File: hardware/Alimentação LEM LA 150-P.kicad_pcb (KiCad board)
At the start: 2 copper layers, 162 x 89 mm, 114 parts, among them J1 USART, J2 RJ45, J3 RJ45, J4 Conn_01x04, J5 Conn_01x04, U1 LM324, U4 ATMEGA328P-PU, U5 MCP2515-xSO, U6 MCP2551-I/SN, U7 LM7805, Y1 16MHz, Y2 16MHz

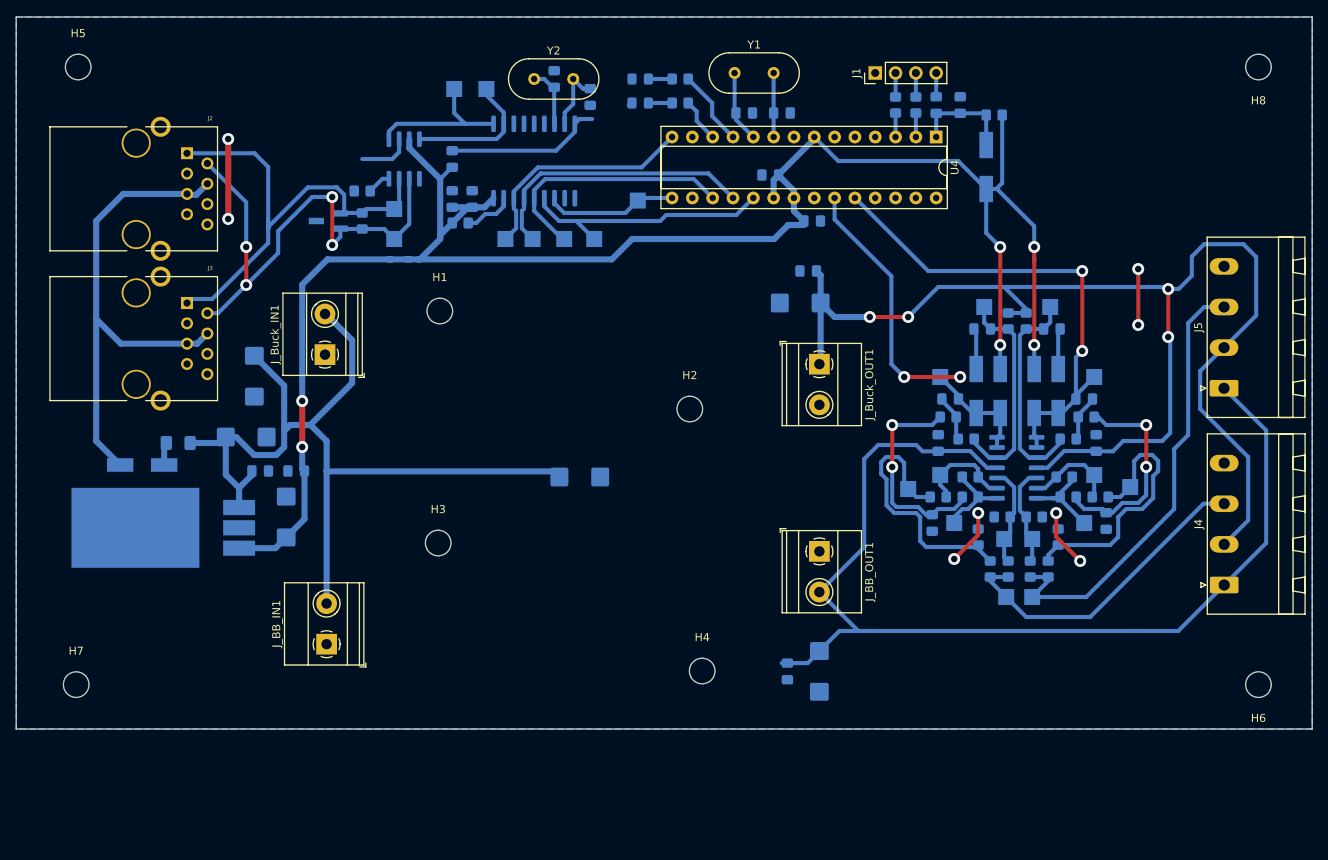
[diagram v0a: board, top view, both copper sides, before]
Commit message: Mudança do conversor 18V -> +/- 15V
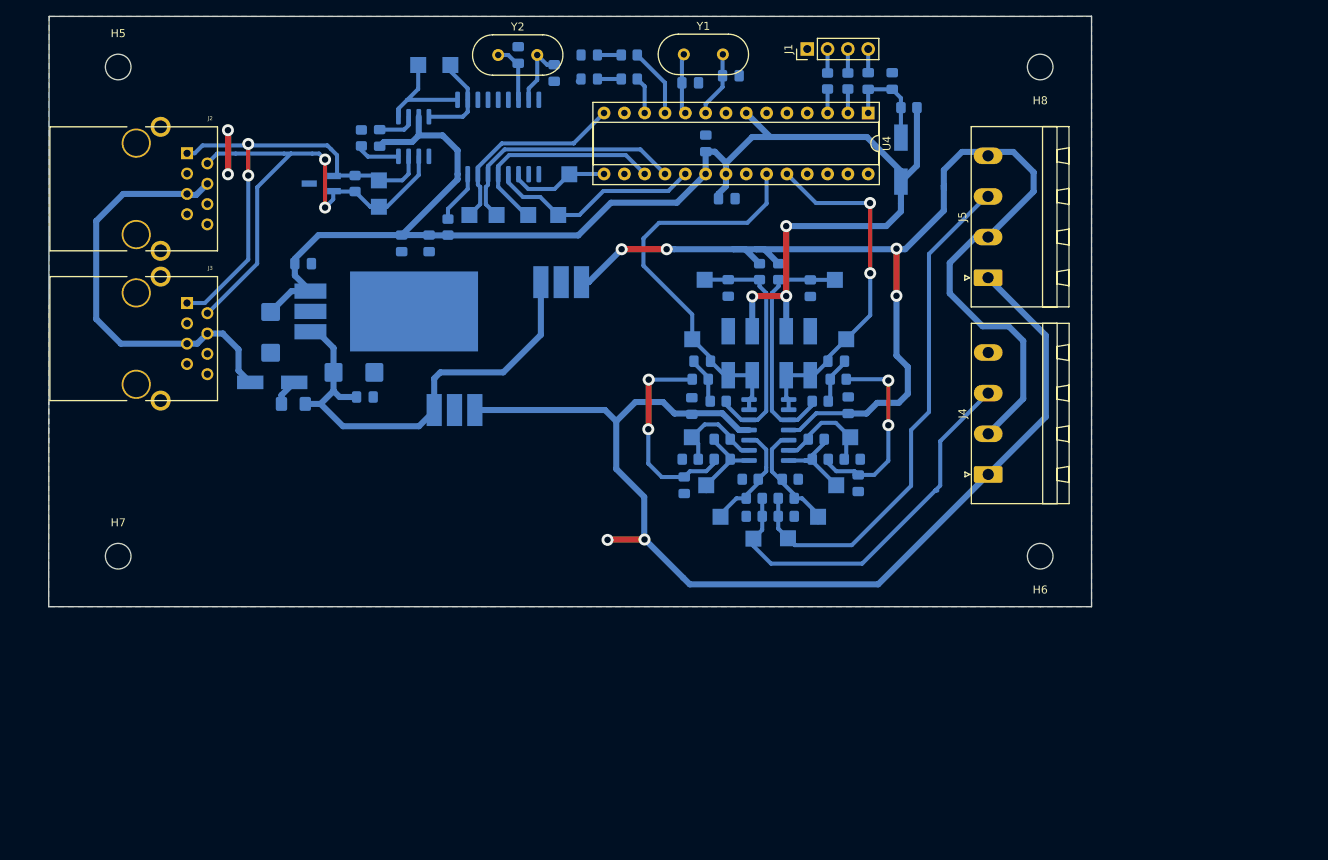
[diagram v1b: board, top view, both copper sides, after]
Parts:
- removed C1, C2: 100n, Capacitor_SMD:C_0805_2012Metric_Pad1.18x1.45mm_HandSolder
- removed C3, C4, C5, C6: 1u, Capacitor_Tantalum_SMD:CP_EIA-6032-20_AVX-F_Pad2.25x2.35mm_HandSolder
- removed H1: Buck_IN+, MountingHole:MountingHole_3.2mm_M3
- removed H2: Buck_Out-1, MountingHole:MountingHole_3.2mm_M3
- removed H3: BBoost_IN+1, MountingHole:MountingHole_3.2mm_M3
- removed H4: BBoost_Out-1, MountingHole:MountingHole_3.2mm_M3
- removed J_BB_IN1, J_BB_OUT1, J_Buck_IN1, J_Buck_OUT1: Screw_Terminal_01x02, TerminalBlock_Phoenix:TerminalBlock_Phoenix_MKDS-1,5-2-5.08_1x02_P5.08mm_Horizontal
- removed R1, R18: 100k, Resistor_SMD:R_0805_2012Metric_Pad1.20x1.40mm_HandSolder
- removed TP1, TP17: in-, TestPoint:TestPoint_Pad_2.0x2.0mm
- added U2: L7815, KicadZeniteSolarLibrary18:TO-220-3_Horizontal_Tabless_SMD, B.Cu at (100.6, 69.4)
- added U3: L7815, KicadZeniteSolarLibrary18:TO-220-3_Horizontal_Tabless_SMD, B.Cu at (87.2, 85.4)
- R23, R5: value 3k9 -> 1k
- moved TP4 35.6 mm to (123.0, 97.5)
- moved TP6 35.1 mm to (121.1, 67.8), turned to 90 degrees
- moved R19 33.4 mm to (131.3, 97.4), turned to 0 degrees
- moved R4 33.0 mm to (127.3, 95.2), turned to 0 degrees
- moved J4 32.6 mm to (156.5, 92.2)
- moved J5 32.6 mm to (156.5, 67.6)
- moved TP2 32.4 mm to (127.2, 100.2)
- moved C12 32.2 mm to (124.0, 68.9), turned to -90 degrees
- moved R6 31.8 mm to (126.8, 92.8)
- moved R21 31.8 mm to (131.3, 95.2), turned to 180 degrees
- moved R27 31.7 mm to (127.9, 66.8)
- moved H6 31.7 mm to (163.0, 102.4)
- moved R28 31.6 mm to (130.3, 66.8)
- moved TP3 31.4 mm to (119.5, 87.5)
- moved TP18 31.4 mm to (131.5, 100.2)
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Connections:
- net /Buck e BuckBoost/+18V_IN renamed /POWER SUPPLY/+18V_OUT
- net /CANBUS/CS renamed /MCU/MCP_SS
- net /CANBUS/INT renamed /MCU/MCP_INT
- net /MCU/analog1 renamed /Bipolar Analog/out1
- net /MCU/analog2 renamed /Bipolar Analog/out2
- net /POWER SUPPLY/+18V_IN renamed /CANBUS CONN/CAN_18V
- R19 pad 2: Net-(R18-Pad1) -> GND
- R2 pad 2: Net-(R1-Pad1) -> GND
- R20 pad 2: Net-(R18-Pad1) -> GND
- R3 pad 2: Net-(R1-Pad1) -> GND
- U4 pad 13: Net-(U4-Pad13) -> unconnected-(U4-Pad13)
- U4 pad 16: Net-(U4-Pad16) -> unconnected-(U4-Pad16)
- U4 pad 25: Net-(U4-Pad25) -> unconnected-(U4-Pad25)
- U4 pad 26: Net-(U4-Pad26) -> unconnected-(U4-Pad26)
- U4 pad 27: Net-(U4-Pad27) -> unconnected-(U4-Pad27)
- U4 pad 28: Net-(U4-Pad28) -> unconnected-(U4-Pad28)
- U4 pad 4: Net-(U4-Pad4) -> unconnected-(U4-Pad4)
- U4 pad 5: Net-(U4-Pad5) -> unconnected-(U4-Pad5)
- U4 pad 6: Net-(U4-Pad6) -> unconnected-(U4-Pad6)
- U5 pad 10: Net-(U5-Pad10) -> unconnected-(U5-Pad10)
- U5 pad 11: Net-(U5-Pad11) -> unconnected-(U5-Pad11)
- U5 pad 3: Net-(U5-Pad3) -> unconnected-(U5-Pad3)
- U5 pad 4: Net-(U5-Pad4) -> unconnected-(U5-Pad4)
- U5 pad 5: Net-(U5-Pad5) -> unconnected-(U5-Pad5)
- U5 pad 6: Net-(U5-Pad6) -> unconnected-(U5-Pad6)
- U6 pad 5: Net-(U6-Pad5) -> unconnected-(U6-Pad5)
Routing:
- net GND: track 68.8 -> 12.2 mm, vias 8 -> 2
- net +5V: track 241.7 -> 186.0 mm, vias 6 -> 3
- net /POWER SUPPLY/+18V_OUT: track 113.6 -> 58.9 mm
- net Net-(R18-Pad1): track 33.5 -> 0.00 mm
- net Net-(R1-Pad1): track 33.5 -> 0.00 mm
- net /Bipolar Analog/out2: track 63.2 -> 44.9 mm
- net /CANBUS CONN/CAN_18V: track 63.4 -> 53.8 mm
- net /Bipolar Analog/in1+: track 39.7 -> 49.0 mm
- net /Bipolar Analog/in2+: track 57.2 -> 64.6 mm
- net /CANBUS/TXCAN: track 19.4 -> 13.8 mm
- net /CANBUS/RXCAN: track 17.2 -> 11.9 mm
- net /SCK: track 32.3 -> 27.0 mm
- net -15V: track 135.4 -> 139.7 mm, vias 0 -> 2
- net /MOSI: track 31.7 -> 27.7 mm
- net /MISO: track 35.0 -> 31.0 mm
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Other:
- board size 162 x 89 mm -> 130.4 x 73.8 mm
- net class Default removed

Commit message: Troca do atmega328p -> STM32F103C8T Já que tem CAN integrado e ADC 12 bits (ao invés de 10)
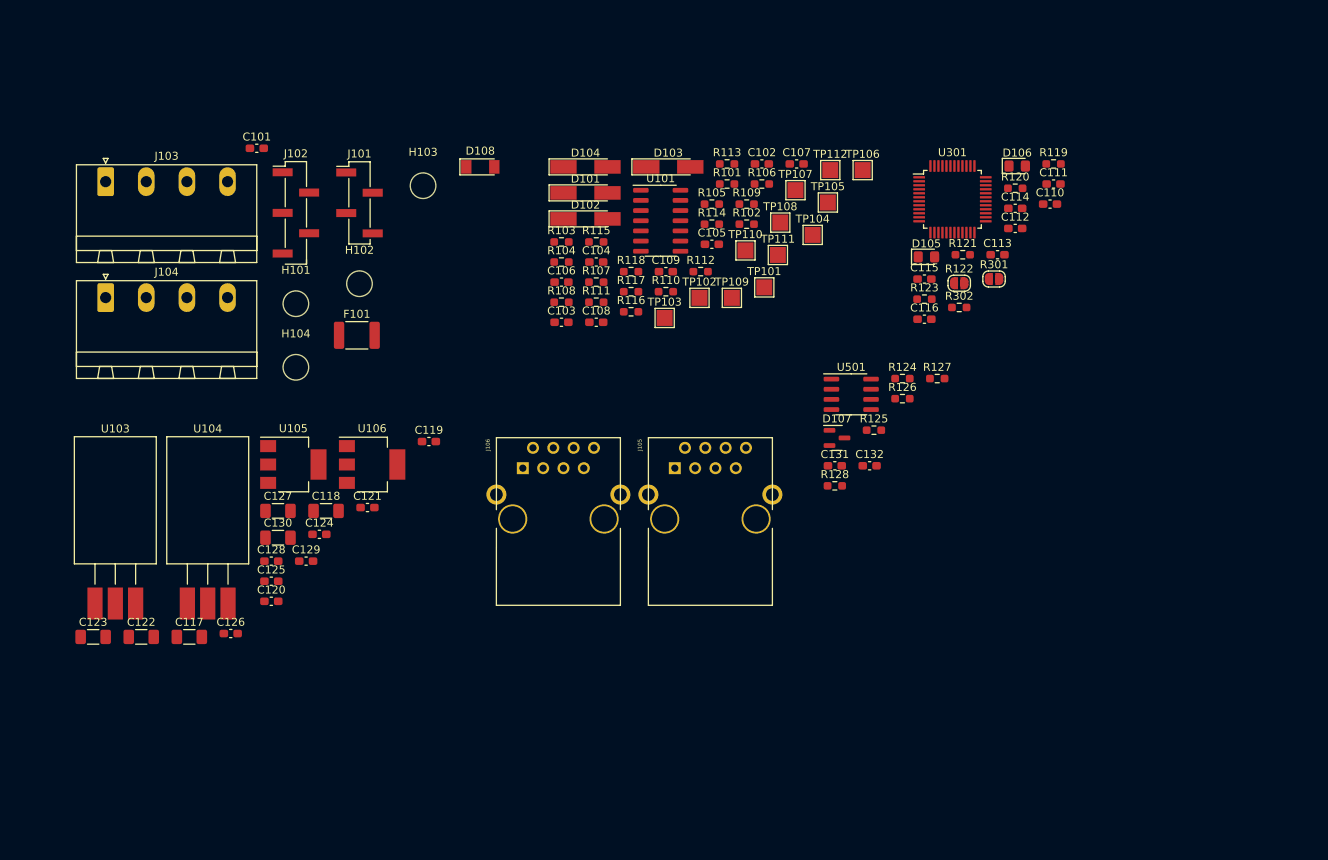
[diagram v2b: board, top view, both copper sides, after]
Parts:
- removed C10, C11, C12, C13, C29, C30, C31, C7: 100n, Capacitor_SMD:C_0805_2012Metric_Pad1.18x1.45mm_HandSolder
- removed C14, C15, C16, C17, C22, C23, C24, C25, C26: 100nF, Capacitor_SMD:C_0805_2012Metric_Pad1.18x1.45mm_HandSolder
- removed C18, C19, C20, C21: 22pF, Capacitor_SMD:C_0805_2012Metric_Pad1.18x1.45mm_HandSolder
- removed C27, C28: 1u, Capacitor_Tantalum_SMD:CP_EIA-6032-20_AVX-F_Pad2.25x2.35mm_HandSolder
- removed D1: pesd1can, Package_TO_SOT_SMD:SOT-23_Handsoldering
- removed D2, D7, D8, D9: 4V7, Diode_SMD:D_MiniMELF_Handsoldering
- removed D3, D6: LL4148, Diode_SMD:D_MiniMELF_Handsoldering
- removed D4, D5: LED_RED, LED_SMD:LED_0805_2012Metric_Pad1.15x1.40mm_HandSolder
- removed F1: 500mA, Fuse:Fuse_1206_3216Metric_Pad1.42x1.75mm_HandSolder
- removed H5: Mount_TL, MountingHole:MountingHole_3.2mm_M3
- removed H6: Mount_TR, MountingHole:MountingHole_3.2mm_M3
- removed H7: Mount_BL, MountingHole:MountingHole_3.2mm_M3
- removed H8: Mount_BR, MountingHole:MountingHole_3.2mm_M3
- removed J1: USART, Connector_PinHeader_2.54mm:PinHeader_1x04_P2.54mm_Vertical
- removed J2, J3: RJ45, KicadZeniteSolarLibrary18:RJ45_YH59_01
- removed J4, J5: Conn_01x04, Connector_Phoenix_MSTB:PhoenixContact_MSTBA_2,5_4-G-5,08_1x04_P5.08mm_Horizontal
- removed R10, R12, R13, R14, R20, R21, R23, R24, R25, R26, R3, R4, R5, R7, R8, R9: 1k, Resistor_SMD:R_0805_2012Metric_Pad1.20x1.40mm_HandSolder
- removed R11, R15: 10k, Resistor_SMD:R_0805_2012Metric_Pad1.20x1.40mm_HandSolder
- removed R16: 4k7, Resistor_SMD:R_0805_2012Metric_Pad1.20x1.40mm_HandSolder
- removed R17: 120, Resistor_SMD:R_0805_2012Metric_Pad1.20x1.40mm_HandSolder
- removed R19, R2: 30, Resistor_SMD:R_0805_2012Metric_Pad1.20x1.40mm_HandSolder
- removed R22, R6: 3k9, Resistor_SMD:R_0805_2012Metric_Pad1.20x1.40mm_HandSolder
- removed R27, R28: 15k, Resistor_SMD:R_0805_2012Metric_Pad1.20x1.40mm_HandSolder
- removed TP10: SO, TestPoint:TestPoint_Pad_2.0x2.0mm
- removed TP11: SI, TestPoint:TestPoint_Pad_2.0x2.0mm
- removed TP12: INT, TestPoint:TestPoint_Pad_2.0x2.0mm
- removed TP13: TXCAN, TestPoint:TestPoint_Pad_2.0x2.0mm
- removed TP14: RXCAN, TestPoint:TestPoint_Pad_2.0x2.0mm
- removed TP15: CAN_H, TestPoint:TestPoint_Pad_2.0x2.0mm
- removed TP16: CAN_L, TestPoint:TestPoint_Pad_2.0x2.0mm
- removed TP18, TP2: in+, TestPoint:TestPoint_Pad_2.0x2.0mm
- removed TP19, TP3: op_a_in-, TestPoint:TestPoint_Pad_2.0x2.0mm
- removed TP20, TP4: op_a_in+, TestPoint:TestPoint_Pad_2.0x2.0mm
- removed TP21, TP5: op_a_out, TestPoint:TestPoint_Pad_2.0x2.0mm
- removed TP22, TP6: op_b_in+, TestPoint:TestPoint_Pad_2.0x2.0mm
- removed TP23, TP7: op_b_out, TestPoint:TestPoint_Pad_2.0x2.0mm
- removed TP8: SCK, TestPoint:TestPoint_Pad_2.0x2.0mm
- removed TP9: SC, TestPoint:TestPoint_Pad_2.0x2.0mm
- removed U1: LM324, Package_SO:SOIC-14_3.9x8.7mm_P1.27mm
- removed U2, U3: L7815, KicadZeniteSolarLibrary18:TO-220-3_Horizontal_Tabless_SMD
- removed U4: ATMEGA328P-PU, Package_DIP:DIP-28_W7.62mm_Socket
- removed U5: MCP2515-xSO, Package_SO:SOIC-18W_7.5x11.6mm_P1.27mm
- removed U6: MCP2551-I/SN, Package_SO:SOIC-8_3.9x4.9mm_P1.27mm
- removed U7: LM7805, KicadZeniteSolarLibrary18:TO-220-3_Horizontal_TabDown_SMD
- removed Y1, Y2: 16MHz, Crystal:Crystal_HC49-U_Vertical
- added C101: 100n, Capacitor_SMD:C_0603_1608Metric_Pad1.08x0.95mm_HandSolder, F.Cu at (65.1, 51.4)
- added C102: 100n, Capacitor_SMD:C_0603_1608Metric_Pad1.08x0.95mm_HandSolder, F.Cu at (128.2, 53.4)
- added C103: 100n, Capacitor_SMD:C_0603_1608Metric_Pad1.08x0.95mm_HandSolder, F.Cu at (103.2, 73.2)
- added C104: 100n, Capacitor_SMD:C_0603_1608Metric_Pad1.08x0.95mm_HandSolder, F.Cu at (107.5, 65.6)
- added C105: 100n, Capacitor_SMD:C_0603_1608Metric_Pad1.08x0.95mm_HandSolder, F.Cu at (122.0, 63.4)
- added C106: 100n, Capacitor_SMD:C_0603_1608Metric_Pad1.08x0.95mm_HandSolder, F.Cu at (103.2, 68.1)
- added C107: 100n, Capacitor_SMD:C_0603_1608Metric_Pad1.08x0.95mm_HandSolder, F.Cu at (132.6, 53.4)
- added C108: 100n, Capacitor_SMD:C_0603_1608Metric_Pad1.08x0.95mm_HandSolder, F.Cu at (107.5, 73.2)
- added C109: 100n, Capacitor_SMD:C_0603_1608Metric_Pad1.08x0.95mm_HandSolder, F.Cu at (116.2, 66.8)
- added C110: 100n, Capacitor_SMD:C_0603_1608Metric_Pad1.08x0.95mm_HandSolder, F.Cu at (164.2, 58.4)
- added C111: 100n, Capacitor_SMD:C_0603_1608Metric_Pad1.08x0.95mm_HandSolder, F.Cu at (164.7, 55.9)
- added C112: 100n, Capacitor_SMD:C_0603_1608Metric_Pad1.08x0.95mm_HandSolder, F.Cu at (159.9, 61.4)
- added C113: 100n, Capacitor_SMD:C_0603_1608Metric_Pad1.08x0.95mm_HandSolder, F.Cu at (157.7, 64.7)
- added C114: 100n, Capacitor_SMD:C_0603_1608Metric_Pad1.08x0.95mm_HandSolder, F.Cu at (159.9, 58.9)
- added C115: 100n, Capacitor_SMD:C_0603_1608Metric_Pad1.08x0.95mm_HandSolder, F.Cu at (148.5, 67.8)
- added C116: 100n, Capacitor_SMD:C_0603_1608Metric_Pad1.08x0.95mm_HandSolder, F.Cu at (148.5, 72.8)
- added C117: 4.7u, Capacitor_SMD:C_1206_3216Metric_Pad1.33x1.80mm_HandSolder, F.Cu at (56.6, 112.5)
- added C118: 4.7u, Capacitor_SMD:C_1206_3216Metric_Pad1.33x1.80mm_HandSolder, F.Cu at (73.7, 96.7)
- added C119: 100n, Capacitor_SMD:C_0603_1608Metric_Pad1.08x0.95mm_HandSolder, F.Cu at (86.6, 88.1)
- added C120: 100n, Capacitor_SMD:C_0603_1608Metric_Pad1.08x0.95mm_HandSolder, F.Cu at (66.9, 108.0)
- added C121: 100n, Capacitor_SMD:C_0603_1608Metric_Pad1.08x0.95mm_HandSolder, F.Cu at (78.9, 96.3)
- added C122: 4.7u, Capacitor_SMD:C_1206_3216Metric_Pad1.33x1.80mm_HandSolder, F.Cu at (50.6, 112.5)
- added C123: 4.7u, Capacitor_SMD:C_1206_3216Metric_Pad1.33x1.80mm_HandSolder, F.Cu at (44.6, 112.5)
- added C124: 100n, Capacitor_SMD:C_0603_1608Metric_Pad1.08x0.95mm_HandSolder, F.Cu at (72.9, 99.7)
- added C125: 100n, Capacitor_SMD:C_0603_1608Metric_Pad1.08x0.95mm_HandSolder, F.Cu at (66.9, 105.5)
- added C126: 100n, Capacitor_SMD:C_0603_1608Metric_Pad1.08x0.95mm_HandSolder, F.Cu at (61.8, 112.1)
- added C127: 4.7u, Capacitor_SMD:C_1206_3216Metric_Pad1.33x1.80mm_HandSolder, F.Cu at (67.7, 96.7)
- added C128: 100n, Capacitor_SMD:C_0603_1608Metric_Pad1.08x0.95mm_HandSolder, F.Cu at (66.9, 103.0)
- added C129: 100n, Capacitor_SMD:C_0603_1608Metric_Pad1.08x0.95mm_HandSolder, F.Cu at (71.2, 103.0)
- added C130: 4.7u, Capacitor_SMD:C_1206_3216Metric_Pad1.33x1.80mm_HandSolder, F.Cu at (67.7, 100.1)
- added C131: 100n, Capacitor_SMD:C_0603_1608Metric_Pad1.08x0.95mm_HandSolder, F.Cu at (137.3, 91.1)
- added C132: 4.7n, Capacitor_SMD:C_0603_1608Metric_Pad1.08x0.95mm_HandSolder, F.Cu at (141.7, 91.1)
- added D101: 3V9, Diode_SMD:D_MiniMELF_Handsoldering, F.Cu at (106.2, 57.0)
- added D102: 3V9, Diode_SMD:D_MiniMELF_Handsoldering, F.Cu at (106.2, 60.2)
- added D103: 3V9, Diode_SMD:D_MiniMELF_Handsoldering, F.Cu at (116.5, 53.7)
- added D104: 3V9, Diode_SMD:D_MiniMELF_Handsoldering, F.Cu at (106.2, 53.7)
- added D105: ~, LED_SMD:LED_0805_2012Metric_Pad1.15x1.40mm_HandSolder, F.Cu at (148.8, 65.0)
- added D106: ~, LED_SMD:LED_0805_2012Metric_Pad1.15x1.40mm_HandSolder, F.Cu at (160.1, 53.6)
- added D107: ~, Package_TO_SOT_SMD:SOT-23, F.Cu at (137.6, 87.6)
- added D108: LL4148, Diode_SMD:D_MiniMELF, F.Cu at (93.0, 53.7)
- added F101: Fuse, Fuse:Fuse_1812_4532Metric_Pad1.30x3.40mm_HandSolder, F.Cu at (77.6, 74.8)
- added H101: Mount_TL, MountingHole:MountingHole_3.2mm_M3, F.Cu at (70.0, 70.8)
- added H102: Mount_TR, MountingHole:MountingHole_3.2mm_M3, F.Cu at (77.9, 68.3)
- added H103: Mount_BL, MountingHole:MountingHole_3.2mm_M3, F.Cu at (85.9, 56.1)
- added H104: Mount_BR, MountingHole:MountingHole_3.2mm_M3, F.Cu at (70.0, 78.8)
- added J101: USART, Connector_PinHeader_2.54mm:PinHeader_1x04_P2.54mm_Vertical_SMD_Pin1Left, F.Cu at (77.9, 58.2)
- added J102: STLink, Connector_PinHeader_2.54mm:PinHeader_1x05_P2.54mm_Vertical_SMD_Pin1Left, F.Cu at (70.0, 59.5)
- added J103: Sensor1, Connector_Phoenix_MSTB:PhoenixContact_MSTBA_2,5_4-G-5,08_1x04_P5.08mm_Horizontal, F.Cu at (46.2, 55.6)
- added J104: Sensor2, Connector_Phoenix_MSTB:PhoenixContact_MSTBA_2,5_4-G-5,08_1x04_P5.08mm_Horizontal, F.Cu at (46.2, 70.1)
- added J105: RJ45, KicadZeniteSolarLibrary18:RJ45_YH59_01, F.Cu at (117.3, 91.4)
- added J106: RJ45, KicadZeniteSolarLibrary18:RJ45_YH59_01, F.Cu at (98.3, 91.4)
- added R101: 30, Resistor_SMD:R_0603_1608Metric_Pad0.98x0.95mm_HandSolder, F.Cu at (123.9, 55.9)
- added R102: 30, Resistor_SMD:R_0603_1608Metric_Pad0.98x0.95mm_HandSolder, F.Cu at (126.3, 60.9)
- added R103: 1k, Resistor_SMD:R_0603_1608Metric_Pad0.98x0.95mm_HandSolder, F.Cu at (103.2, 63.1)
- added R104: 1k, Resistor_SMD:R_0603_1608Metric_Pad0.98x0.95mm_HandSolder, F.Cu at (103.2, 65.6)
- added R105: 1k, Resistor_SMD:R_0603_1608Metric_Pad0.98x0.95mm_HandSolder, F.Cu at (122.0, 58.4)
- added R106: 1k, Resistor_SMD:R_0603_1608Metric_Pad0.98x0.95mm_HandSolder, F.Cu at (128.2, 55.9)
- added R107: 1k, Resistor_SMD:R_0603_1608Metric_Pad0.98x0.95mm_HandSolder, F.Cu at (107.5, 68.1)
- added R108: 3k9, Resistor_SMD:R_0603_1608Metric_Pad0.98x0.95mm_HandSolder, F.Cu at (103.2, 70.6)
- added R109: 3k9, Resistor_SMD:R_0603_1608Metric_Pad0.98x0.95mm_HandSolder, F.Cu at (126.3, 58.4)
- added R110: 1k, Resistor_SMD:R_0603_1608Metric_Pad0.98x0.95mm_HandSolder, F.Cu at (116.2, 69.3)
- added R111: 1k, Resistor_SMD:R_0603_1608Metric_Pad0.98x0.95mm_HandSolder, F.Cu at (107.5, 70.6)
- added R112: 1k, Resistor_SMD:R_0603_1608Metric_Pad0.98x0.95mm_HandSolder, F.Cu at (120.6, 66.8)
- added R113: 1k, Resistor_SMD:R_0603_1608Metric_Pad0.98x0.95mm_HandSolder, F.Cu at (123.9, 53.4)
- added R114: 1k, Resistor_SMD:R_0603_1608Metric_Pad0.98x0.95mm_HandSolder, F.Cu at (122.0, 60.9)
- added R115: 1k, Resistor_SMD:R_0603_1608Metric_Pad0.98x0.95mm_HandSolder, F.Cu at (107.5, 63.1)
- added R116: 1k, Resistor_SMD:R_0603_1608Metric_Pad0.98x0.95mm_HandSolder, F.Cu at (111.9, 71.8)
- added R117: 15k, Resistor_SMD:R_0603_1608Metric_Pad0.98x0.95mm_HandSolder, F.Cu at (111.9, 69.3)
- added R118: 15k, Resistor_SMD:R_0603_1608Metric_Pad0.98x0.95mm_HandSolder, F.Cu at (111.9, 66.8)
- added R119: 10k, Resistor_SMD:R_0603_1608Metric_Pad0.98x0.95mm_HandSolder, F.Cu at (164.7, 53.4)
- added R120: 10k, Resistor_SMD:R_0603_1608Metric_Pad0.98x0.95mm_HandSolder, F.Cu at (159.9, 56.4)
- added R121: 10k, Resistor_SMD:R_0603_1608Metric_Pad0.98x0.95mm_HandSolder, F.Cu at (153.3, 64.7)
- added R122: BOOT0, Jumper:SolderJumper-2_P1.3mm_Open_RoundedPad1.0x1.5mm, F.Cu at (152.9, 68.3)
- added R123: 10k, Resistor_SMD:R_0603_1608Metric_Pad0.98x0.95mm_HandSolder, F.Cu at (148.5, 70.3)
- added R124: 4k7, Resistor_SMD:R_0603_1608Metric_Pad0.98x0.95mm_HandSolder, F.Cu at (145.8, 80.2)
- added R125: NC, Resistor_SMD:R_0603_1608Metric_Pad0.98x0.95mm_HandSolder, F.Cu at (142.2, 86.6)
- added R126: 300, Resistor_SMD:R_0603_1608Metric_Pad0.98x0.95mm_HandSolder, F.Cu at (145.8, 82.7)
- added R127: 520, Resistor_SMD:R_0603_1608Metric_Pad0.98x0.95mm_HandSolder, F.Cu at (150.1, 80.2)
- added R128: 520, Resistor_SMD:R_0603_1608Metric_Pad0.98x0.95mm_HandSolder, F.Cu at (137.3, 93.6)
- added R301: JUMP0, Jumper:SolderJumper-2_P1.3mm_Open_RoundedPad1.0x1.5mm, F.Cu at (157.2, 67.7)
- added R302: 10k, Resistor_SMD:R_0603_1608Metric_Pad0.98x0.95mm_HandSolder, F.Cu at (152.9, 71.3)
- added TP101: in+, TestPoint:TestPoint_Pad_2.0x2.0mm, F.Cu at (128.5, 68.8)
- added TP102: in+, TestPoint:TestPoint_Pad_2.0x2.0mm, F.Cu at (120.4, 70.1)
- added TP103: op_a_in-, TestPoint:TestPoint_Pad_2.0x2.0mm, F.Cu at (116.1, 72.6)
- added TP104: op_a_in+, TestPoint:TestPoint_Pad_2.0x2.0mm, F.Cu at (134.6, 62.2)
- added TP105: op_a_in-, TestPoint:TestPoint_Pad_2.0x2.0mm, F.Cu at (136.5, 58.2)
- added TP106: op_a_in+, TestPoint:TestPoint_Pad_2.0x2.0mm, F.Cu at (140.8, 54.1)
- added TP107: op_a_out, TestPoint:TestPoint_Pad_2.0x2.0mm, F.Cu at (132.4, 56.6)
- added TP108: op_a_out, TestPoint:TestPoint_Pad_2.0x2.0mm, F.Cu at (130.5, 60.7)
- added TP109: op_b_in+, TestPoint:TestPoint_Pad_2.0x2.0mm, F.Cu at (124.5, 70.1)
- added TP110: op_b_in+, TestPoint:TestPoint_Pad_2.0x2.0mm, F.Cu at (126.2, 64.2)
- added TP111: op_b_out, TestPoint:TestPoint_Pad_2.0x2.0mm, F.Cu at (130.2, 64.7)
- added TP112: op_b_out, TestPoint:TestPoint_Pad_2.0x2.0mm, F.Cu at (136.8, 54.1)
- added U101: LM324, Package_SO:SOIC-14_3.9x8.7mm_P1.27mm, F.Cu at (115.6, 60.5)
- added U103: K78L15-1000R3, KicadZeniteSolarLibrary18:TO-220-3_Horizontal_Tabless_SMD, F.Cu at (44.8, 107.0)
- added U104: K78L15-1000R3, KicadZeniteSolarLibrary18:TO-220-3_Horizontal_Tabless_SMD, F.Cu at (56.4, 107.0)
- added U105: AMS1117-5, Package_TO_SOT_SMD:SOT-223-3_TabPin2, F.Cu at (69.6, 90.9)
- added U106: AMS1117-3.3, Package_TO_SOT_SMD:SOT-223-3_TabPin2, F.Cu at (79.5, 90.9)
- added U301: STM32F103C8Tx, Package_QFP:LQFP-48_7x7mm_P0.5mm, F.Cu at (152.0, 57.8)
- added U501: MCP2561-E-SN, Package_SO:SOIC-8_3.9x4.9mm_P1.27mm, F.Cu at (139.4, 82.2)
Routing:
- net +5V: track 186.0 -> 0.00 mm, vias 3 -> 0
- net +15V: track 156.7 -> 0.00 mm, vias 4 -> 0
- net -15V: track 139.7 -> 0.00 mm, vias 2 -> 0
- net /Bipolar Analog/in2+: track 64.6 -> 0.00 mm
- net /CANBUS CONN/CAN_L: track 63.8 -> 0.00 mm, vias 2 -> 0
- net /CANBUS CONN/CAN_H: track 60.7 -> 0.00 mm, vias 2 -> 0
- net /POWER SUPPLY/+18V_OUT: track 58.9 -> 0.00 mm
- net /CANBUS CONN/CAN_18V: track 53.8 -> 0.00 mm
- net /Bipolar Analog/out1: track 50.4 -> 0.00 mm
- net /Bipolar Analog/in1+: track 49.0 -> 0.00 mm
- net /Bipolar Analog/out2: track 44.9 -> 0.00 mm, vias 2 -> 0
- net Net-(C31-Pad1): track 31.4 -> 0.00 mm
- net /MISO: track 31.0 -> 0.00 mm
- net Net-(C12-Pad1): track 30.3 -> 0.00 mm
- net /MOSI: track 27.7 -> 0.00 mm
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- removed copper zone on B.Cu, net GND
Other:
- board outline removed

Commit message: Primeiro protótipo da PCB
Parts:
- added TP501: TxCAN, TestPoint:TestPoint_Pad_2.0x2.0mm, B.Cu at (125.1, 72.4)
- added TP502: RxCAN, TestPoint:TestPoint_Pad_2.0x2.0mm, B.Cu at (126.4, 75.6)
- added TP503: CAN_H, TestPoint:TestPoint_Pad_2.0x2.0mm, B.Cu at (118.9, 84.8)
- added TP504: CAN_L, TestPoint:TestPoint_Pad_2.0x2.0mm, B.Cu at (124.0, 84.8)
- C102, C103, C104, C105, C106, C107, C108, C109, C110, C111, C112, C113, C114, C115, C116, C118, C120, C123, C125, C131, C132, D101, D102, D103, D104, D105, D106, R101, R102, R103, R104, R105, R106, R107, R108, R109, R110, R111, R112, R113, R114, R115, R116, R117, R118, R119, R120, R121, R122, R123, R124, R125, R126, R127, R128, R301, R302, TP101, TP102, TP103, TP104, TP105, TP106, TP107, TP108, TP109, TP110, TP111, TP112, U101, U104, U301, U501: moved to B.Cu
- D107: value ~ -> pesd1can; moved to B.Cu
- moved J104 147.4 mm to (184.9, 119.9), turned to 90 degrees
- moved J103 143.8 mm to (184.9, 93.5), turned to 90 degrees
- moved H104 131.1 mm to (190.5, 130.5)
- moved H103 105.2 mm to (190.5, 67.2)
- moved C101 90.3 mm to (151.8, 76.8), turned to 90 degrees
- moved J102 87.9 mm to (156.2, 76.2)
- moved C122 83.8 mm to (134.4, 111.8)
- moved C123 83.7 mm to (128.3, 108.6), turned to -90 degrees
- moved U103 79.1 mm to (123.8, 111.7)
- moved C126 77.5 mm to (137.7, 96.5), turned to -90 degrees
- moved C130 74.5 mm to (141.0, 86.4), turned to -90 degrees
- moved R103 74.0 mm to (165.2, 103.5), turned to -90 degrees
- moved C129 73.5 mm to (142.9, 86.4), turned to -90 degrees
- moved R104 73.1 mm to (162.9, 107.7), turned to 90 degrees
- moved J101 70.1 mm to (146.7, 71.8)
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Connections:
- U301 pad 10: /Bipolar Analog/out1 -> unconnected-(U301-Pad10)
- U301 pad 11: /Bipolar Analog/out2 -> unconnected-(U301-Pad11)
- U301 pad 13: unconnected-(U301-Pad13) -> /Bipolar Analog/out2
- U301 pad 14: unconnected-(U301-Pad14) -> /Bipolar Analog/out1
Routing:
- net GND: track 0.00 -> 131.7 mm, vias 0 -> 4
- net +15V: track 0.00 -> 84.8 mm, vias 0 -> 7
- net +3V3: track 0.00 -> 79.3 mm, vias 0 -> 2
- net -15V: track 0.00 -> 56.0 mm, vias 0 -> 2
- net +5V: track 0.00 -> 50.9 mm, vias 0 -> 1
- net /CANBUS CONN/CAN_H: track 0.00 -> 49.6 mm, vias 0 -> 2
- net /CANBUS CONN/CAN_18V: track 0.00 -> 49.2 mm
- net /Bipolar Analog/out1: track 0.00 -> 47.9 mm
- net /CANBUS CONN/CAN_L: track 0.00 -> 45.5 mm
- net /Bipolar Analog/out2: track 0.00 -> 40.4 mm
- net /STM32/USART1_RX: track 0.00 -> 25.5 mm, vias 0 -> 1
- net /POWER SUPPLY/+18V: track 0.00 -> 19.6 mm, vias 0 -> 1
- net /CANBUS/CAN_TX: track 0.00 -> 18.3 mm
- net /STM32/USART1_TX: track 0.00 -> 18.0 mm, vias 0 -> 1
- net Net-(R107-Pad1): track 0.00 -> 16.5 mm, vias 0 -> 2
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- added copper zone on B.Cu, net GND
- added copper zone on F.Cu, net GND
